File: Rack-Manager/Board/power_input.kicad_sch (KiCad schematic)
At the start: 23 parts, among them J1 ARJM11C7-114-BA-EW2, J2 USB4105-GT-A, U1 Ag9712-FL, U2 TPS259470A, U3 TPS259470A

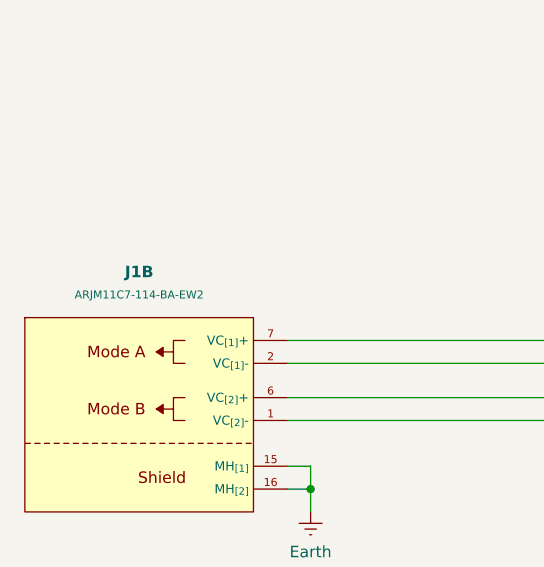
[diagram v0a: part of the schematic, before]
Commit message: Updated Texas Instruments and WIZnet KiCAD libraries. Continued with the schematics design.
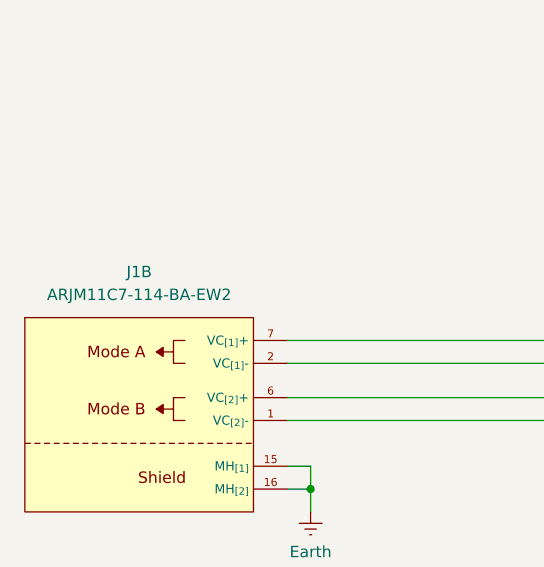
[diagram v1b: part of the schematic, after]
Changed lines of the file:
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@@
 				(font
 					(size 1.27 1.27)
-					(thickness 0.254)
-					(bold yes)
 				)
 			)
@@
 			(effects
 				(font
-					(size 0.889 0.889)
+					(size 1.27 1.27)
 				)
 			)
@@
 		)
 		(instances
-			(project "Rack-Manager"
+			(project ""
+				(path "/5d42174d-da49-4bca-870b-353868af7168/781970e2-2116-4faf-b2d3-2243f6c2f5bb"
+					(reference "J1")
+					(unit 2)
+				)
 				(path "/5d42174d-da49-4bca-870b-353868af7168/b63ba99b-295c-4c28-a131-5e86bb9173d4"
 					(reference "J1")

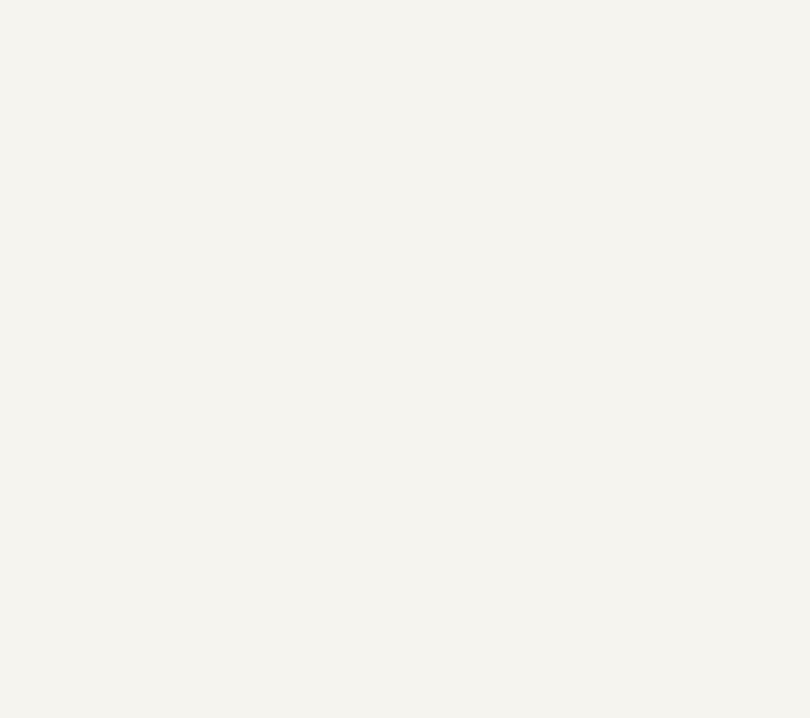
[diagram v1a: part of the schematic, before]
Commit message: Updated Texas Instruments KiCAD library. Continued with the schematics design.
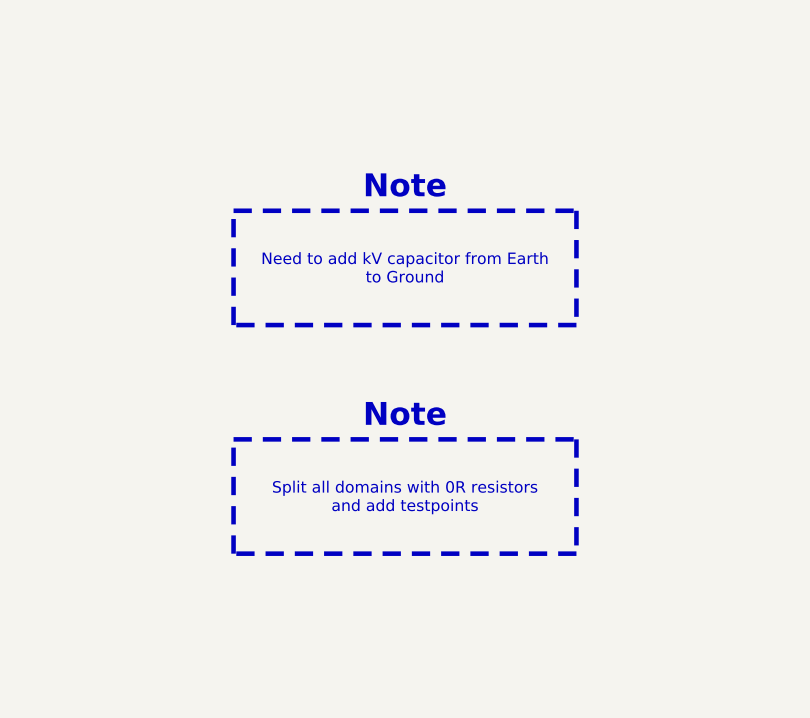
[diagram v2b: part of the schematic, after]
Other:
- note added: "Note"
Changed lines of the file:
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@@
+		)
+	)
+	(text "Note"
+		(exclude_from_sim no)
+		(at 234.95 200.66 0)
+		(effects
+			(font
+				(size 2.54 2.54)
+				(thickness 0.508)
+				(bold yes)
+				(color 194 0 0 1)
+			)
+		)
+	)
+	(text "Note"
+		(exclude_from_sim no)
+		(at 234.95 226.06 0)
+		(effects
+			(font
+				(size 2.54 2.54)
+				(thickness 0.508)
+				(bold yes)
+				(color 194 0 0 1)
+			)
 		)
 	)
@@
 		)
 	)
+	(text_box "Need to add kV capacitor from Earth to Ground"
+		(exclude_from_sim no)
+		(at 215.9 203.2 0)
+		(size 38.1 12.7)
+		(margins 0.9525 0.9525 0.9525 0.9525)
+		(stroke
+			(width 0.508)
+			(type dot)
+			(color 194 0 0 1)
+		)
+		(fill
+			(type color)
+			(color 255 165 169 1)
+		)
+		(effects
+			(font
+				(size 1.27 1.27)
+			)
+		)
+	)
 	(text_box "OVLO = 17V\nUVLO = 4V\n"
 		(exclude_from_sim no)
@@
 		)
 		(effects
+			(font
+				(size 1.27 1.27)
+			)
+		)
+	)
+	(text_box "Split all domains with 0R resistors and add testpoints"
+		(exclude_from_sim no)
+		(at 215.9 228.6 0)
+		(size 38.1 12.7)
+		(margins 0.9525 0.9525 0.9525 0.9525)
+		(stroke
+			(width 0.508)
+			(type dot)
+			(color 194 0 0 1)
+		)
+		(fill
+			(type color)
+			(color 255 165 169 1)
+		)
+		(effects

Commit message: Continued with the schematic drawing.
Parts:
- removed C4: ~, Capacitor_SMD:C_0402_1005Metric, symbol Device:C_Small
- added C3, C5, C6: ~, Capacitor_SMD:C_0603_1608Metric, symbol Device:C_Small
- C4: renamed from C3; footprint Capacitor_SMD:C_0402_1005Metric -> Capacitor_SMD:C_0603_1608Metric; now fitted
- renumbered C5 to C7, C6 to C8
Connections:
- net GND: now also C3.2, C5.2, C6.2
- net at C4.1, U3.7 (dV/dT): now also C3.1
- net at U2.7 (dV/dT): now also C5.1, C6.1
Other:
- moved on the sheet: C1, C2, R10, R11

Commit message: Added Bourns library, updated Texas Instruments library, continued with schematic drawing.
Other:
- note removed: "Note"
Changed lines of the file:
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@@
-		)
-	)
-	(text "Note"
-		(exclude_from_sim no)
-		(at 234.95 200.66 0)
-		(effects
-			(font
-				(size 2.54 2.54)
-				(thickness 0.508)
-				(bold yes)
-				(color 194 0 0 1)
-			)
-		)
-	)
-	(text "Note"
-		(exclude_from_sim no)
-		(at 234.95 226.06 0)
-		(effects
-			(font
-				(size 2.54 2.54)
-				(thickness 0.508)
-				(bold yes)
-				(color 194 0 0 1)
-			)
 		)
 	)
@@
 		)
 	)
-	(text "Note"
+	(text_box "400uF @ ( dT=1ms  dV=10mV  I=4A )"
 		(exclude_from_sim no)
-		(at 234.95 251.46 0)
-		(effects
-			(font
-				(size 2.54 2.54)
-				(thickness 0.508)
-				(bold yes)
-				(color 194 0 0 1)
-			)
-		)
-	)
-	(text_box "400uF @ (DT=1ms DV=10mV I=4A)"
-		(exclude_from_sim no)
-		(at 118.11 238.76 0)
-		(size 38.1 3.81)
+		(at 115.57 240.03 0)
+		(size 43.18 3.81)
 		(margins 0.9525 0.9525 0.9525 0.9525)
 		(stroke
@@
 		)
 	)
-	(text_box "Need to add kV capacitor from Earth to Ground"
-		(exclude_from_sim no)
-		(at 215.9 203.2 0)
-		(size 38.1 12.7)
-		(margins 0.9525 0.9525 0.9525 0.9525)
-		(stroke
-			(width 0.508)
-			(type dot)
-			(color 194 0 0 1)
-		)
-		(fill
-			(type color)
-			(color 255 165 169 1)
-		)
-		(effects
-			(font
-				(size 1.27 1.27)
-			)
-		)
-	)
-	(text_box "Need to add dV/dT capacitor to limit in-rush current"
-		(exclude_from_sim no)
-		(at 215.9 254 0)
-		(size 38.1 12.7)
-		(margins 0.9525 0.9525 0.9525 0.9525)
-		(stroke
-			(width 0.508)
-			(type dot)
-			(color 194 0 0 1)
-		)
-		(fill
-			(type color)
-			(color 255 165 169 1)
-		)
-		(effects
-			(font
-				(size 1.27 1.27)
-			)
-		)
-	)
 	(text_box "OVLO = 17V\nUVLO = 4V\n"
 		(exclude_from_sim no)
-		(at 125.73 83.82 0)
+		(at 125.73 85.09 0)
 		(size 15.24 6.35)
 		(margins 0.9525 0.9525 0.9525 0.9525)
@@
 	(text_box "I_{Timer} = 100ms\nI_{LIM} = 0.93A\ndV/dT = 0.5A"
 		(exclude_from_sim no)
-		(at 266.7 172.72 0)
+		(at 266.7 173.99 0)
 		(size 50.8 8.89)
 		(margins 0.9525 0.9525 0.9525 0.9525)
@@
 		)
 	)
-	(text_box "Split all domains with 0R resistors and add testpoints"
-		(exclude_from_sim no)
-		(at 215.9 228.6 0)
-		(size 38.1 12.7)
-		(margins 0.9525 0.9525 0.9525 0.9525)
-		(stroke
-			(width 0.508)
-			(type dot)
-			(color 194 0 0 1)
-		)
-		(fill
-			(type color)
-			(color 255 165 169 1)
-		)
-		(effects
-			(font
-				(size 1.27 1.27)
-			)
-		)
-	)
 	(text_box "I_{Timer} = 100ms\nI_{LIM} = 4.0A\ndV/dT = 2.0A"
 		(exclude_from_sim no)
-		(at 177.8 83.82 0)
+		(at 177.8 85.09 0)
 		(size 50.8 8.89)
 		(margins 0.9525 0.9525 0.9525 0.9525)

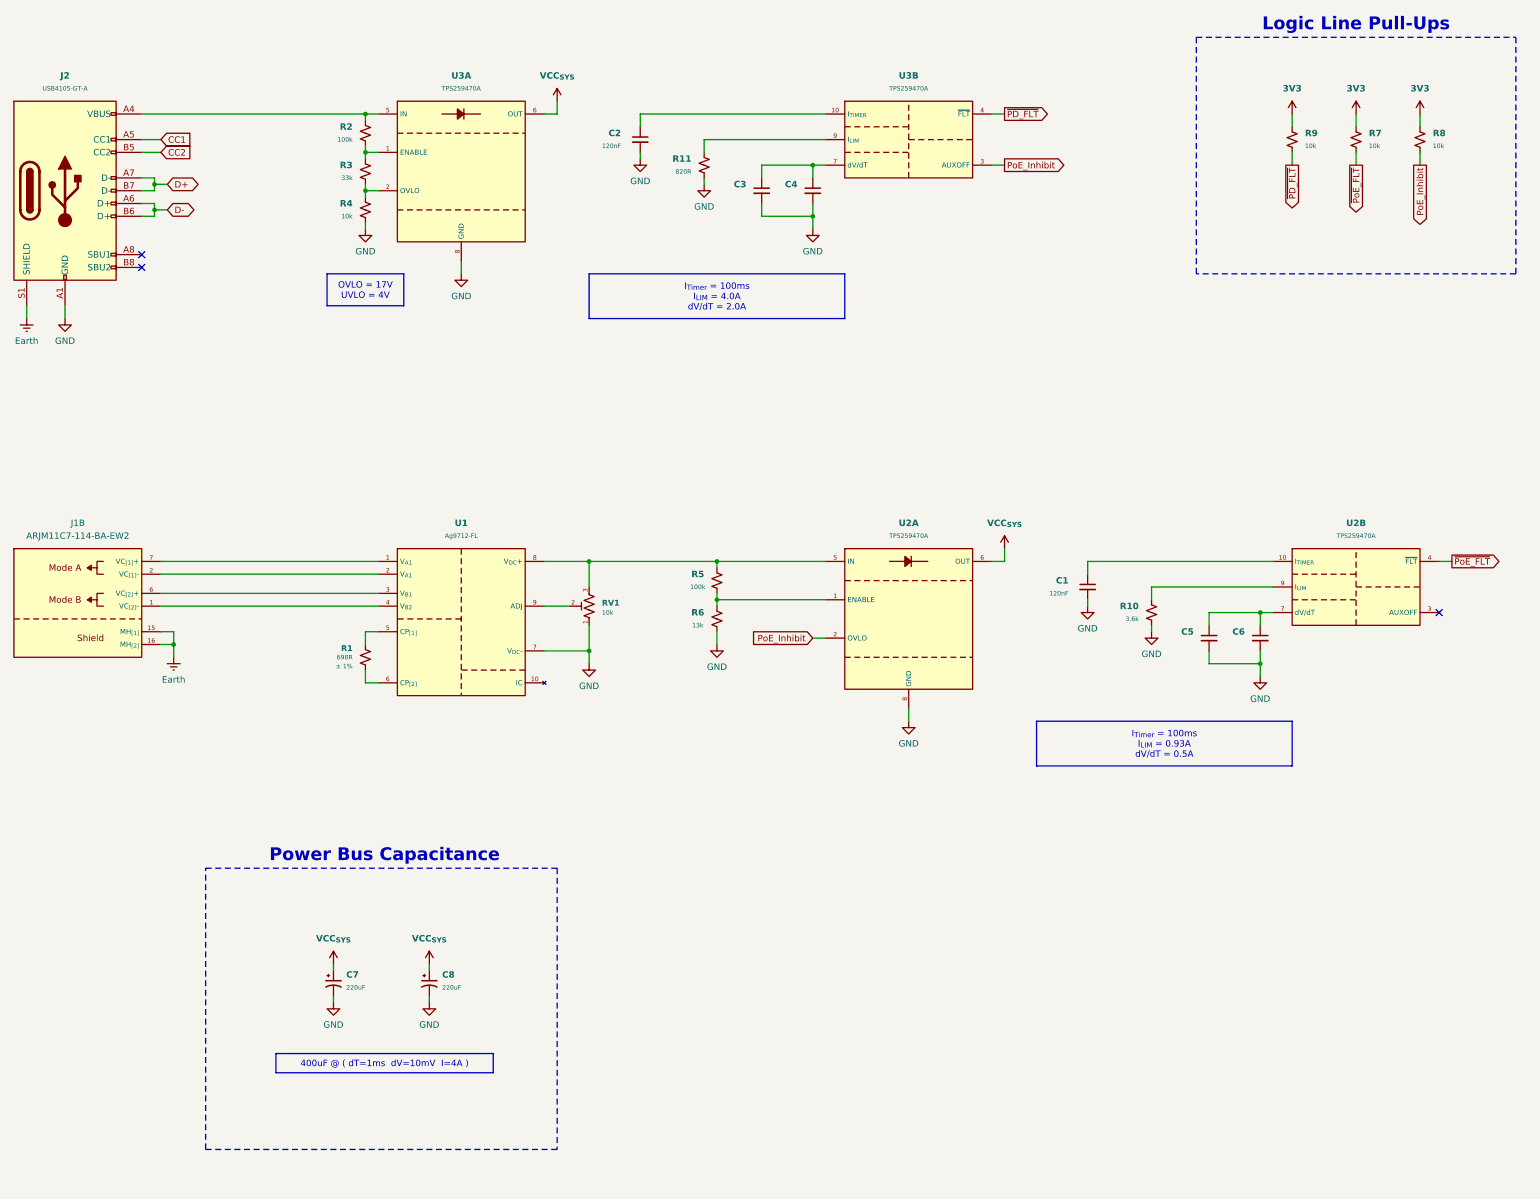
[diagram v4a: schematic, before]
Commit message: Added dvdt cap on eFuses and choose PD standalone sink controller
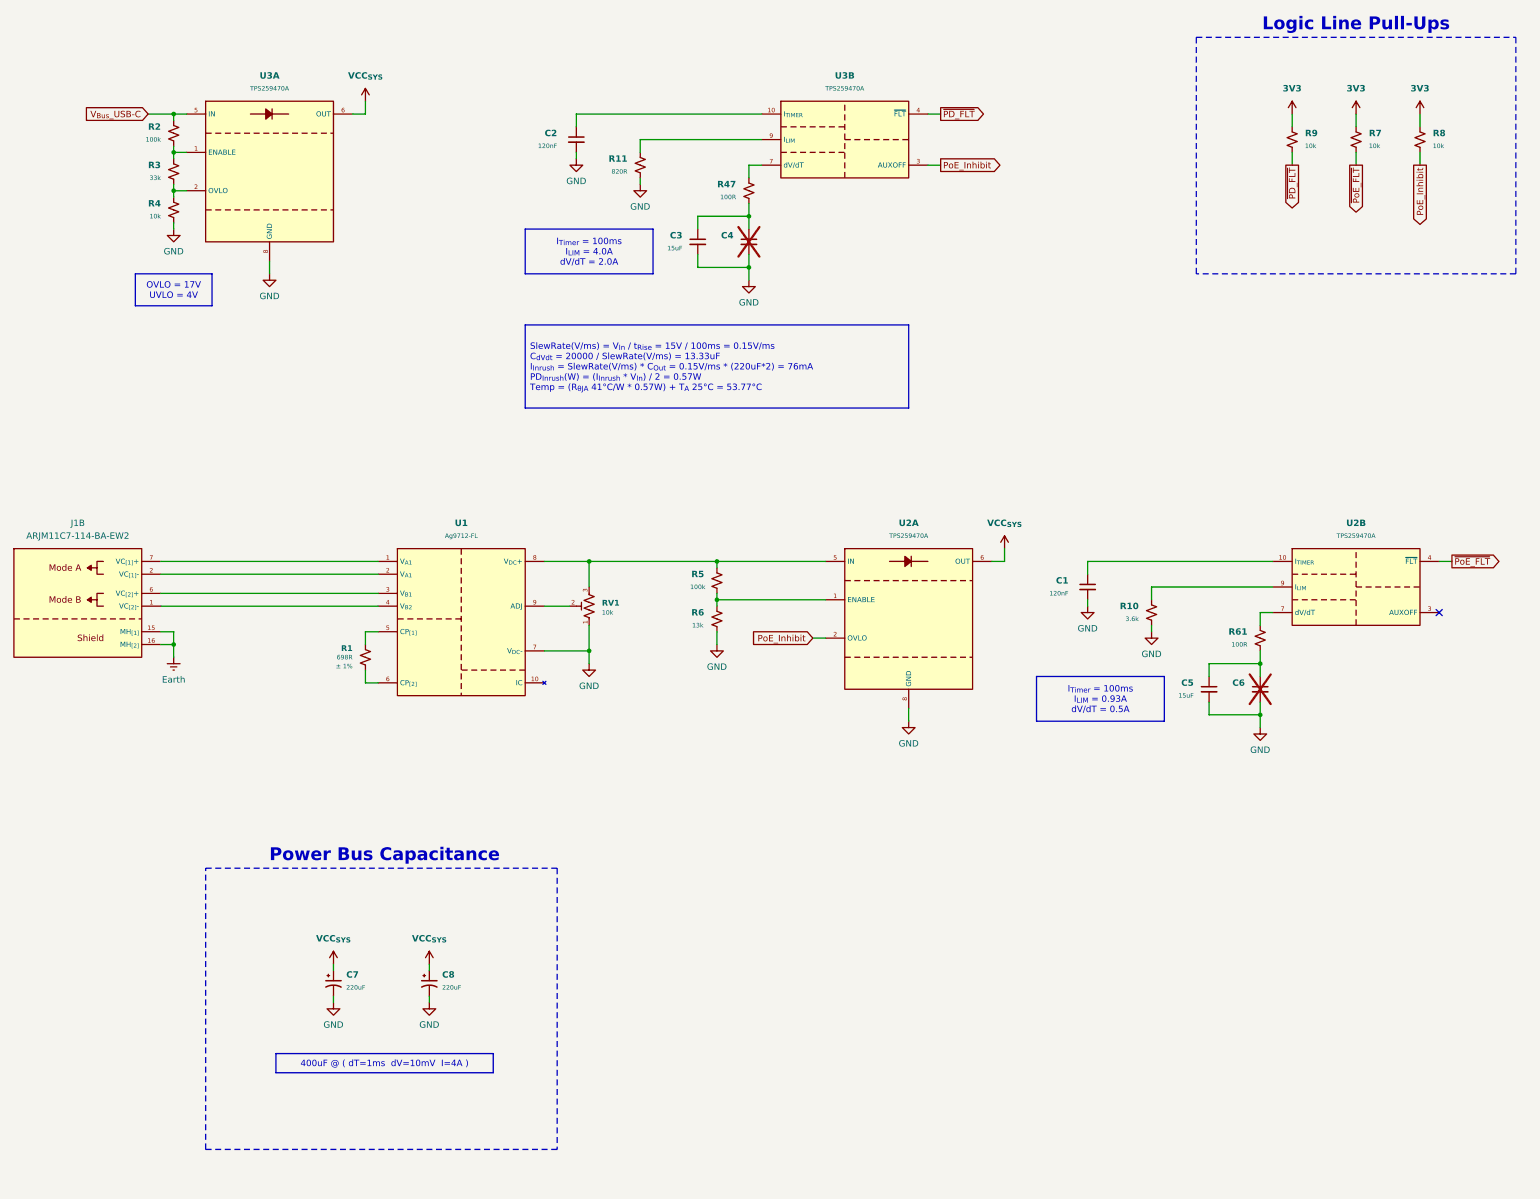
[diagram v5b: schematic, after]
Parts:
- removed J2: USB4105-GT-A, Connector_USB:USB_C_Receptacle_GCT_USB4105-xx-A_16P_TopMnt_Horizontal, symbol Connector:USB_C_Receptacle_USB2.0_16P
- added R47, R61: 100R, Resistor_SMD:R_0402_1005Metric, symbol Device:R_Small_US
- C3, C5: value ~ -> 15uF; footprint Capacitor_SMD:C_0603_1608Metric -> Capacitor_SMD:C_0805_2012Metric
- C4, C6: footprint Capacitor_SMD:C_0603_1608Metric -> Capacitor_SMD:C_0805_2012Metric; now not fitted
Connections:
- net V_{Bus}_USB-C: now reaches R2.1, U3.5 (IN)
- net at C3.1, C4.1: now also R47.2; no longer U3.7 (dV/dT)
- net at C5.1, C6.1: now also R61.2; no longer U2.7 (dV/dT)
- new net: R61.1, U2.7 (dV/dT)
- new net: R47.1, U3.7 (dV/dT)
- no-connect marks 3 -> 1
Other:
- moved on the sheet: C2, C3, R11, R2, R3, R4, U3A, U3B

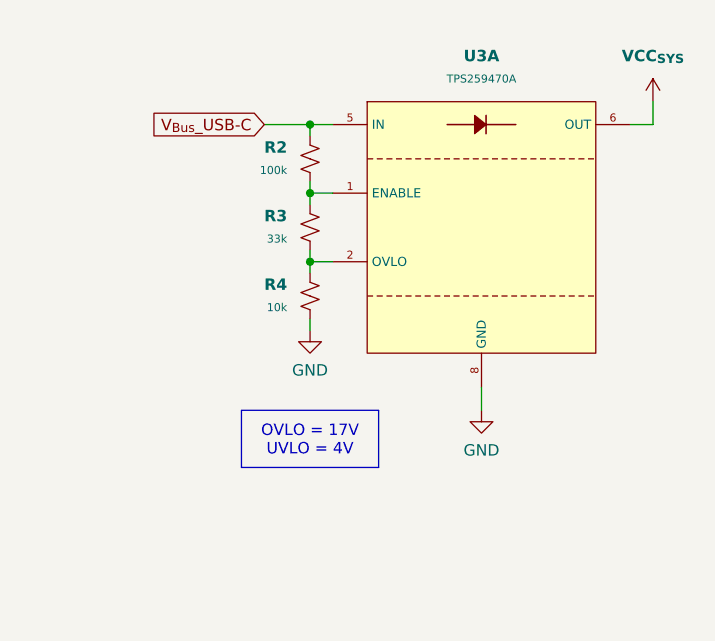
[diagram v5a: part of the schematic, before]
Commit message: Added MCU, Fixed USB-C PD Ideal Diode bug and updated the todo notes
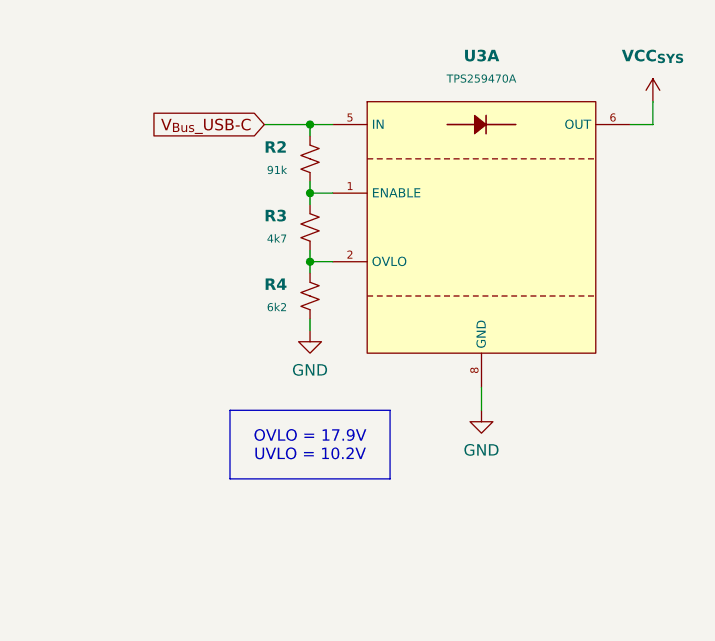
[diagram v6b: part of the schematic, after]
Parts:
- R2: value 100k -> 91k
- R3: value 33k -> 4k7
- R4: value 10k -> 6k2
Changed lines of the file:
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@@
 		)
 	)
-	(text_box "OVLO = 17V\nUVLO = 4V\n"
+	(text_box "OVLO = 17.9V\nUVLO = 10.2V\n"
 		(exclude_from_sim no)
-		(at 87.63 85.09 0)
-		(size 15.24 6.35)
+		(at 86.36 85.09 0)
+		(size 17.78 7.62)
 		(margins 0.9525 0.9525 0.9525 0.9525)
 		(stroke
@@
 			)
 		)
-		(property "Value" "100k"
+		(property "Value" "91k"
 			(at 92.71 58.42 0)
 			(effects
@@
 			)
 		)
-		(property "Value" "10k"
+		(property "Value" "6k2"
 			(at 92.71 73.66 0)
 			(effects
@@
 			)
 		)
-		(property "Value" "33k"
+		(property "Value" "4k7"
 			(at 92.71 66.04 0)
 			(effects
